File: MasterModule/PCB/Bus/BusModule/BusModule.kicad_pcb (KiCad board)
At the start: 2 copper layers, 6 parts

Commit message: [MasterModule][PCB] Add full traced BUS circuit board
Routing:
- net +12V: track 0.00 -> 95.2 mm
- net /CAN_H: track 0.00 -> 85.0 mm
- net GND: track 0.00 -> 50.9 mm
- net /CAN_L: track 0.00 -> 44.2 mm
- net (no net): vias 0 -> 4

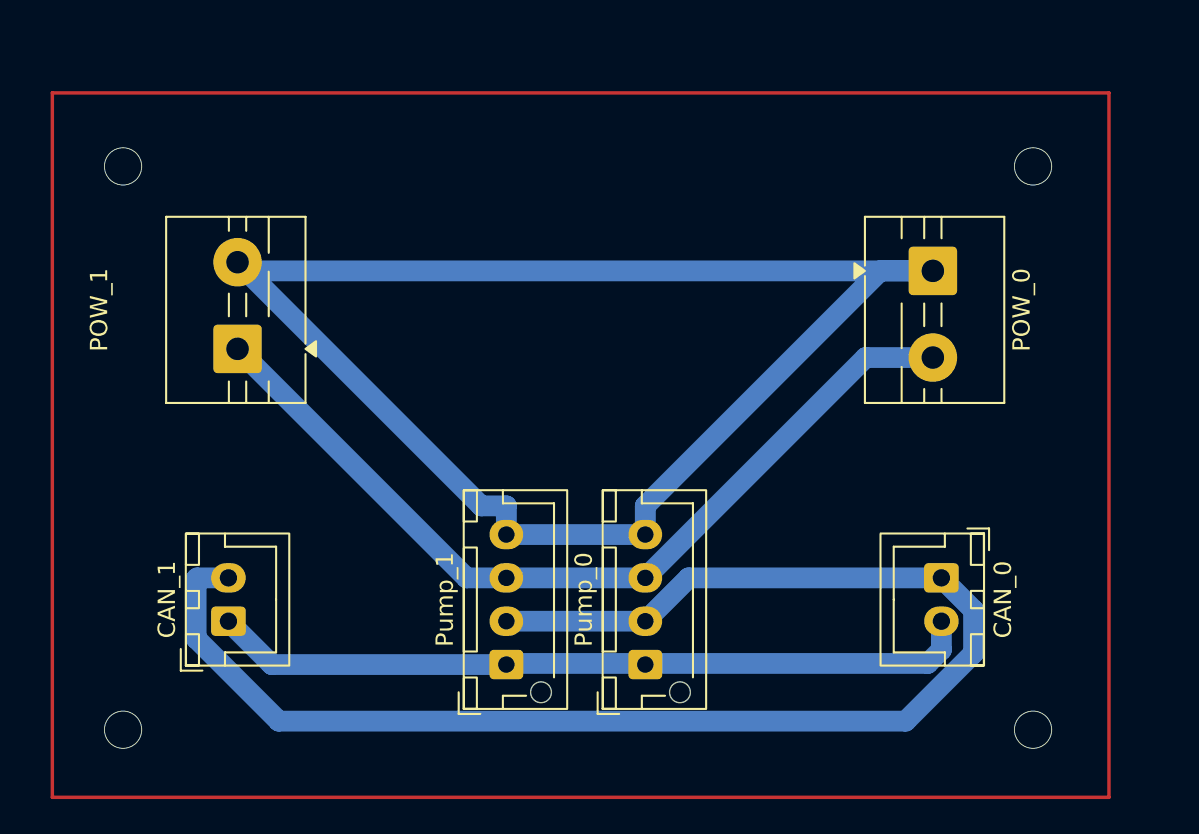
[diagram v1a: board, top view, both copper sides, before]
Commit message: [BUS][PCB] Fix chipboard size
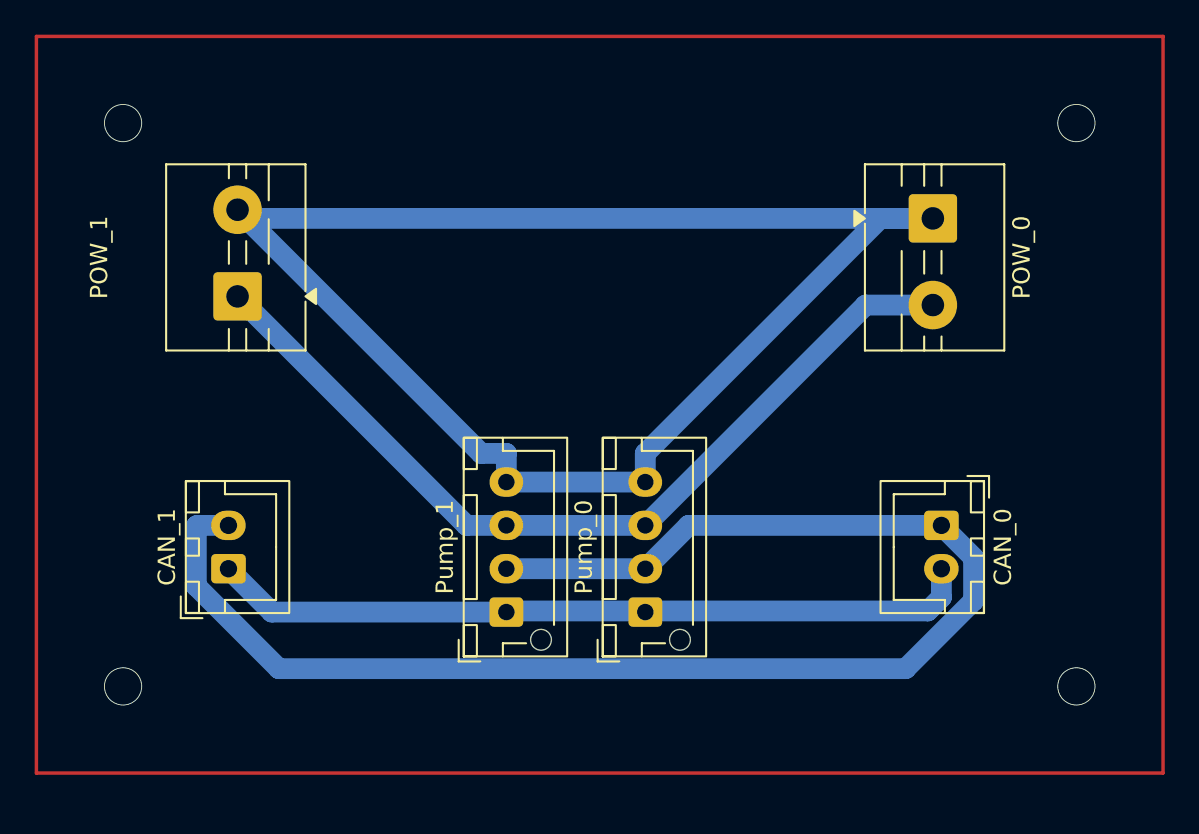
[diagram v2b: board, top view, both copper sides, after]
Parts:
- moved POW_0 3.03 mm to (109.2, 55.5)
- moved POW_1 3.03 mm to (69.1, 60.0)
- moved CAN_0 3.03 mm to (109.7, 73.2)
- moved CAN_1 3.03 mm to (68.6, 75.7)
- moved Pump_0 3.03 mm to (92.6, 78.2)
- moved Pump_1 3.03 mm to (84.6, 78.2)

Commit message: [BUS][PCB] Made PCB template for manufacturing
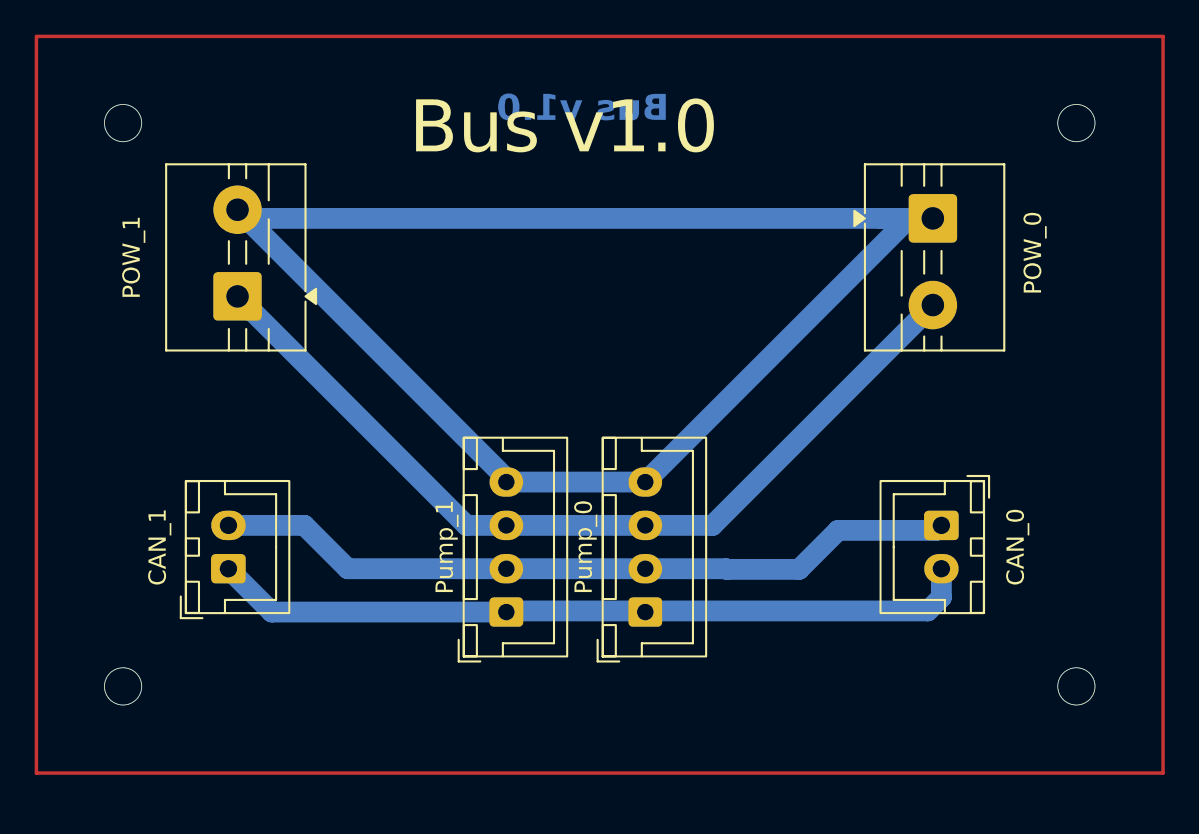
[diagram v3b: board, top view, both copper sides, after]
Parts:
- Pump_0, Pump_1: footprint Connector_JST:JST_XH_B4B-XH-AM_1x04_P2.50mm_Vertical -> Connector_JST:JST_XH_B4B-XH-A_1x04_P2.50mm_Vertical
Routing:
- net /CAN_H: track 85.0 -> 43.2 mm
- net +12V: track 95.2 -> 96.4 mm
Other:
- board text added: "Bus v1.0"
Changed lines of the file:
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@@
 		(filling no)
 		(pcbplotparams
-			(layerselection 0x00000000_00000000_55555555_5755f5ff)
+			(layerselection 0x00000000_00000000_55555555_55555570)
 			(plot_on_all_layers_selection 0x00000000_00000000_00000000_00000000)
 			(disableapertmacros no)
@@
 			(plotframeref no)
 			(mode 1)
-			(useauxorigin no)
+			(useauxorigin yes)
 			(pdf_front_fp_property_popups yes)
 			(pdf_back_fp_property_popups yes)
@@
 			(dxfimperialunits yes)
 			(dxfusepcbnewfont yes)
-			(psnegative no)
+			(psnegative yes)
 			(psa4output no)
 			(plot_black_and_white yes)
@@
 			(crossoutdnponfab yes)
 			(subtractmaskfromsilk no)
-			(outputformat 1)
+			(outputformat 4)
 			(mirror no)
-			(drillshape 1)
+			(drillshape 0)
 			(scaleselection 1)
-			(outputdirectory "")
+			(outputdirectory "Manufacturing/")
 		)
 	)
@@
 		(tags "THT terminal block MaiXu MX126-5.0-02P pitch 5mm size 10.5x7.8mm drill 1.3mm pad 2.8mm")
 		(property "Reference" "POW_0"
-			(at 2.25 -5.12 90)
+			(at 2 -5.78 90)
 			(layer "F.SilkS")
 			(effects
@@
 		)
 	)
-	(footprint "Connector_JST:JST_XH_B4B-XH-AM_1x04_P2.50mm_Vertical"
+	(footprint "Connector_JST:JST_XH_B4B-XH-A_1x04_P2.50mm_Vertical"
 		(layer "F.Cu")
 		(at 84.613 78.212 90)
-		(descr "JST XH series connector, B4B-XH-AM, with boss (http://www.jst-mfg.com/product/pdf/eng/eXH.pdf)")
-		(tags "connector JST XH vertical boss")
+		(descr "JST XH series connector, B4B-XH-A (http://www.jst-mfg.com/product/pdf/eng/eXH.pdf)")
+		(tags "connector JST XH vertical")
 		(property "Reference" "Pump_1"
 			(at 3.75 -3.55 90)
@@
 		(fp_line
 			(start -1.8 -0.2)
-			(end -1.8 1.14)
+			(end -1.8 2.75)
 			(stroke
 				(width 0.12)
@@
 		)
 		(fp_line
-			(start 3.75 2.75)
-			(end -0.74 2.75)
+			(start -1.8 2.75)
+			(end 3.75 2.75)
 			(stroke
 				(width 0.12)
@@
 				)
 			)
-		)
-		(pad "" np_thru_hole circle
-			(at -1.6 2 90)
-			(size 1.2 1.2)
-			(drill 1.2)
-			(layers "*.Cu" "*.Mask")
 		)
 		(pad "1" thru_hole roundrect
@@
 		)
 		(embedded_fonts no)
-		(model "${KICAD10_3DMODEL_DIR}/Connector_JST.3dshapes/JST_XH_B4B-XH-AM_1x04_P2.50mm_Vertical.step"
+		(model "${KICAD10_3DMODEL_DIR}/Connector_JST.3dshapes/JST_XH_B4B-XH-A_1x04_P2.50mm_Vertical.step"
 			(offset
 				(xyz 0 0 0)
@@
 		(tags "connector JST XH vertical")
 		(property "Reference" "CAN_0"
-			(at 1.25 -3.55 90)
+			(at 1.25 -4.2875 90)
 			(layer "F.SilkS")
 			(effects
@@
 		)
 	)
-	(footprint "Connector_JST:JST_XH_B4B-XH-AM_1x04_P2.50mm_Vertical"
+	(footprint "Connector_JST:JST_XH_B4B-XH-A_1x04_P2.50mm_Vertical"
 		(layer "F.Cu")
 		(at 92.6295 78.212 90)
-		(descr "JST XH series connector, B4B-XH-AM, with boss (http://www.jst-mfg.com/product/pdf/eng/eXH.pdf)")
-		(tags "connector JST XH vertical boss")
+		(descr "JST XH series connector, B4B-XH-A (http://www.jst-mfg.com/product/pdf/eng/eXH.pdf)")
+		(tags "connector JST XH vertical")
 		(property "Reference" "Pump_0"
 			(at 3.75 -3.55 90)
@@
 		(fp_line
 			(start -1.8 -0.2)
-			(end -1.8 1.14)
+			(end -1.8 2.75)
 			(stroke
 				(width 0.12)
@@
 		)
 		(fp_line
-			(start 3.75 2.75)
-			(end -0.74 2.75)
+			(start -1.8 2.75)
+			(end 3.75 2.75)
 			(stroke
 				(width 0.12)
@@
 				)
 			)
-		)
-		(pad "" np_thru_hole circle
-			(at -1.6 2 90)
-			(size 1.2 1.2)
-			(drill 1.2)
-			(layers "*.Cu" "*.Mask")
 		)
 		(pad "1" thru_hole roundrect
@@
 		)
 		(embedded_fonts no)
-		(model "${KICAD10_3DMODEL_DIR}/Connector_JST.3dshapes/JST_XH_B4B-XH-AM_1x04_P2.50mm_Vertical.step"
+		(model "${KICAD10_3DMODEL_DIR}/Connector_JST.3dshapes/JST_XH_B4B-XH-A_1x04_P2.50mm_Vertical.step"
 			(offset
 				(xyz 0 0 0)
@@
 		(tags "connector JST XH vertical")
 		(property "Reference" "CAN_1"
-			(at 1.25 -3.55 90)
+			(at 1.25 -4.08 90)
 			(layer "F.SilkS")
 			(effects
@@
 		(tags "THT terminal block MaiXu MX126-5.0-02P pitch 5mm size 10.5x7.8mm drill 1.3mm pad 2.8mm")
 		(property "Reference" "POW_1"
-			(at 2.25 -7.984 90)
+			(at 2.25 -6.105 90)
 			(layer "F.SilkS")
 			(effects
@@
 		(layer "F.Cu")
 	)
+	(gr_text "Bus v1.0"
+		(at 94 50 0)
+		(layer "B.Cu")
+		(effects
+			(font
+				(size 1.5 1.5)
+				(thickness 0.3)
+				(bold yes)
+			)
+			(justify left bottom mirror)
+		)
+	)
+	(gr_text "Bus v1.0"
+		(at 79 52 0)
+		(layer "F.SilkS")
+		(effects
+			(font
+				(size 3 3)
+				(thickness 0.4)
+			)
+			(justify left bottom)
+		)
+	)
 	(dimension
 		(type orthogonal)
@@
 			(keep_text_aligned yes)
 		)
-		(gr_text "42.5"
+		(gr_text "42,5"
 			(at 48.85 66.25 90)
 			(layer "User.1")
@@
 			(keep_text_aligned yes)
 		)
-		(gr_text "32.5"
+		(gr_text "32,5"
 			(at 128.85 66.25 90)
 			(layer "User.1")
@@
 	)
 	(segment
-		(start 84.613 70.712)
-		(end 84.613 69.0603)
-		(width 1.2)
-		(layer "B.Cu")
-		(net "+12V")
-	)
-	(segment
-		(start 92.6295 70.712)
-		(end 92.6295 69.0603)
-		(width 1.2)
-		(layer "B.Cu")
-		(net "+12V")
-	)
-	(segment
-		(start 106.1898 55.5)
-		(end 92.6295 69.0603)
-		(width 1.2)
-		(layer "B.Cu")
-		(net "+12V")
-	)
-	(segment
-		(start 83.1653 69.0603)
-		(end 84.613 69.0603)
+		(start 107.8415 55.5)
+		(end 92.6295 70.712)
 		(width 1.2)
 		(layer "B.Cu")
@@
 	)
 	(segment
-		(start 69.105 55)
-		(end 83.1653 69.0603)
-		(width 1.2)
-		(layer "B.Cu")
-		(net "+12V")
-	)
-	(segment
 		(start 109.22 55.5)
 		(end 106.1898 55.5)
@@
 	)
 	(segment
+		(start 84.613 70.508)
+		(end 69.105 55)
+		(width 1.2)
+		(layer "B.Cu")
+		(net "+12V")
+	)
+	(segment
 		(start 69.605 55.5)
 		(end 69.105 55)
@@
 	)
 	(segment
-		(start 105.3415 60.5)
+		(start 84.613 70.712)
+		(end 84.613 70.508)
+		(width 1.2)
+		(layer "B.Cu")
+		(net "+12V")
+	)
+	(segment
+		(start 109.22 55.5)
+		(end 107.8415 55.5)
+		(width 1.2)
+		(layer "B.Cu")
+		(net "+12V")
+	)
+	(segment
+		(start 96.508 73.212)
 		(end 92.6295 73.212)
 		(width 1.2)
@@
 	(segment
 		(start 109.22 60.5)
-		(end 105.3415 60.5)
+		(end 96.508 73.212)
 		(width 1.2)
 		(layer "B.Cu")
@@
 	)
 	(segment
-		(start 92.6295 75.712)
-		(end 95.1295 73.212)
+		(start 103.75 73.5)
+		(end 109.4245 73.5)
 		(width 1.2)
 		(layer "B.Cu")
@@
 	)
 	(segment
-		(start 66.7203 76.7131)
-		(end 66.7203 73.27)
+		(start 97.288 75.712)
+		(end 97.326 75.75)
 		(width 1.2)
 		(layer "B.Cu")
@@
 	)
 	(segment
-		(start 109.7125 73.212)
-		(end 111.5684 75.0679)
+		(start 109.4245 73.5)
+		(end 109.7125 73.212)
 		(width 1.2)
 		(layer "B.Cu")
@@
 	)
 	(segment
-		(start 71.484 81.4768)
-		(end 66.7203 76.7131)
+		(start 75.462 75.712)
+		(end 72.962 73.212)
 		(width 1.2)
 		(layer "B.Cu")
@@
 	)
 	(segment
-		(start 66.7203 73.27)
-		(end 66.7783 73.212)
-		(width 1.2)
-		(layer "B.Cu")
-		(net "/CAN_H")
-	)
-	(segment
-		(start 111.5684 77.5603)
-		(end 107.6519 81.4768)
+		(start 84.613 75.712)
+		(end 75.462 75.712)
 		(width 1.2)
 		(layer "B.Cu")
@@
 	)
 	(segment
-		(start 111.5684 75.0679)
-		(end 111.5684 77.5603)
+		(start 101.5 75.75)
+		(end 103.75 73.5)
 		(width 1.2)
 		(layer "B.Cu")
@@
 	)
 	(segment
-		(start 95.1295 73.212)
-		(end 109.7125 73.212)
+		(start 92.6295 75.712)
+		(end 97.288 75.712)
 		(width 1.2)
 		(layer "B.Cu")
@@
 	)
 	(segment
-		(start 68.58 73.212)
-		(end 66.7783 73.212)
+		(start 72.962 73.212)
+		(end 68.58 73.212)
 		(width 1.2)
 		(layer "B.Cu")
@@
 	)
 	(segment
-		(start 107.6519 81.4768)
-		(end 71.484 81.4768)
-		(width 1.2)
-		(layer "B.Cu")
+		(start 97.326 75.75)
+		(end 101.5 75.75)
+		(width 1.2)
+		(layer "B.Cu")
